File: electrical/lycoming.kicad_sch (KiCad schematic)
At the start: 30 parts

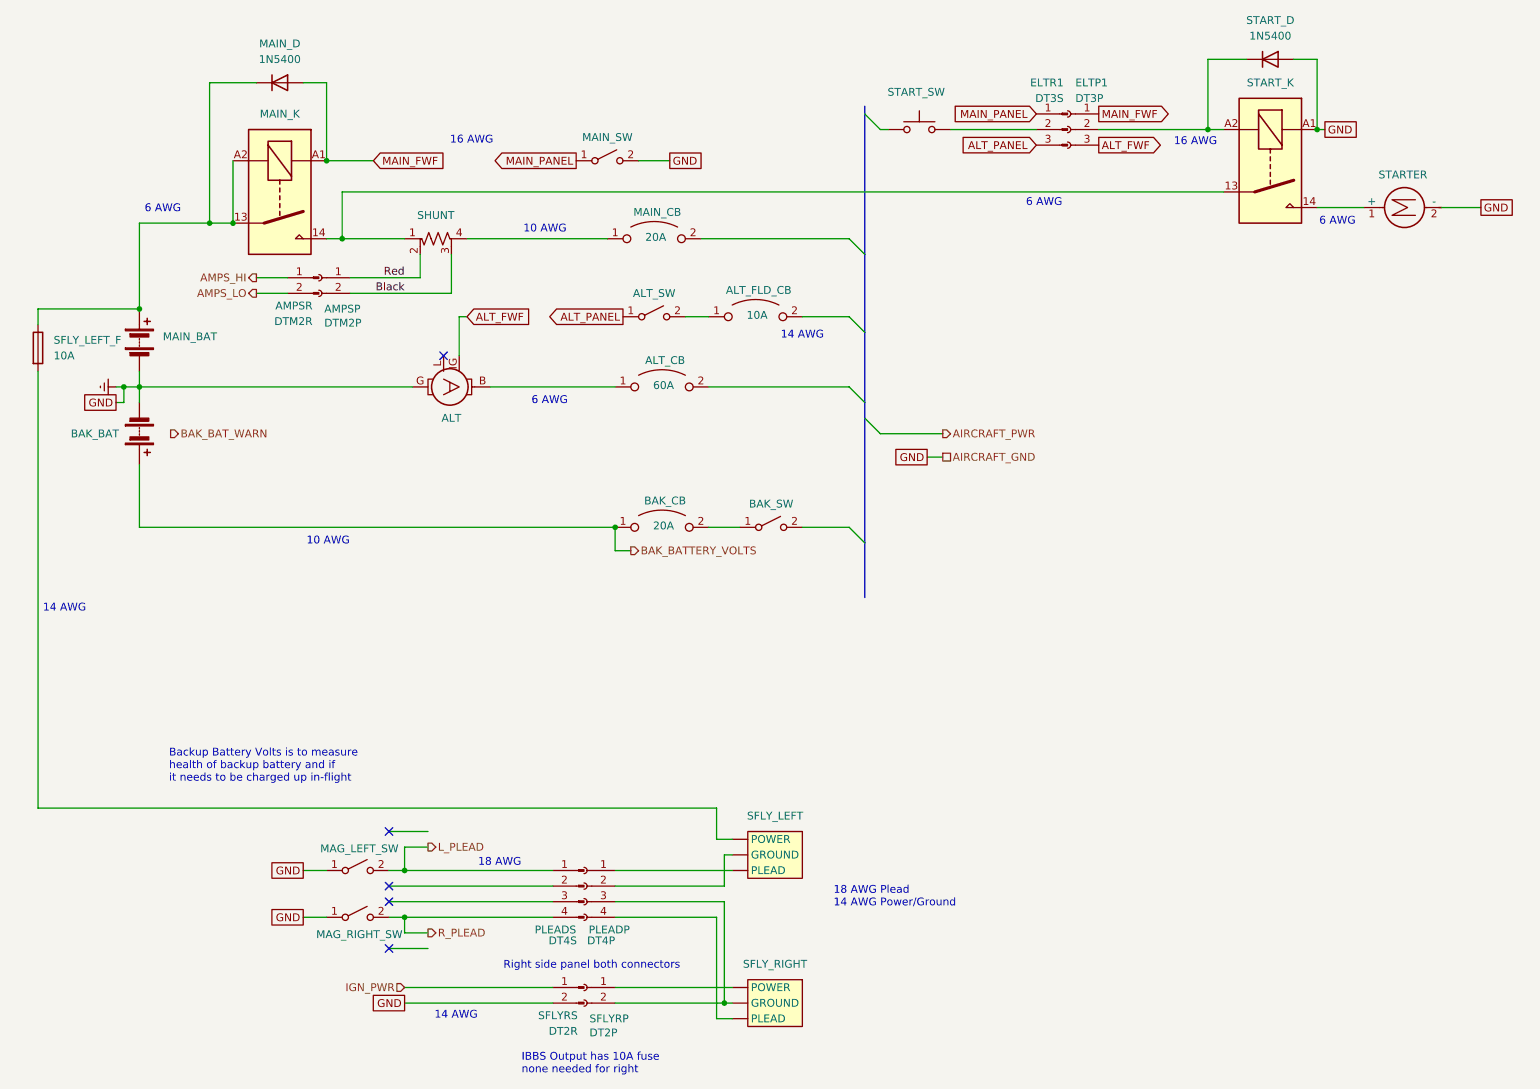
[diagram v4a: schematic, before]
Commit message: Assumed engine connector is sufficient for wiring on bench..
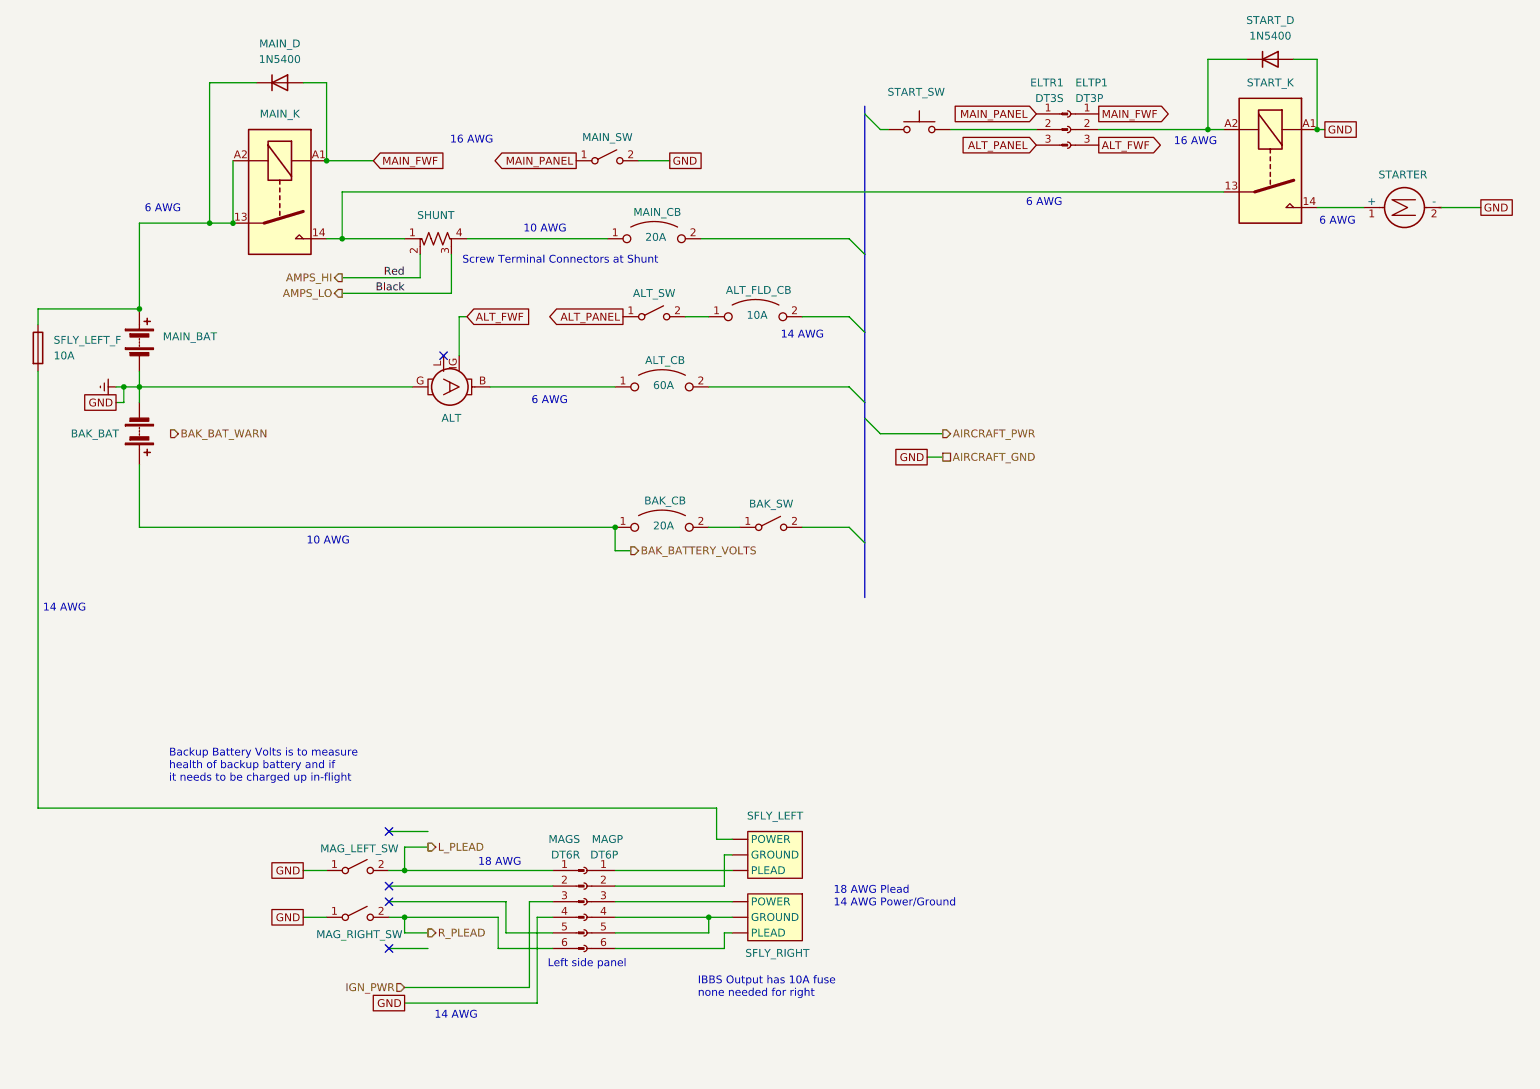
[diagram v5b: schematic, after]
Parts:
- removed AMPSP: DTM2P, symbol Connector:Conn_01x02_Socket
- removed AMPSR: DTM2R, symbol Connector:Conn_01x02_Pin
- removed PLEADP: DT4P, symbol Connector:Conn_01x04_Socket
- removed PLEADS: DT4S, symbol Connector:Conn_01x04_Pin
- removed SFLYRP: DT2P, symbol Connector:Conn_01x02_Socket
- removed SFLYRS: DT2R, symbol Connector:Conn_01x02_Pin
- added MAGP: DT6P, symbol Connector:Conn_01x06_Socket
- added MAGS: DT6R, symbol Connector:Conn_01x06_Pin
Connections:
- net Black is gone; now on net AMPS_LO: SHUNT.3
- net Red is gone; now on net AMPS_HI: SHUNT.2
- net Earth: now also MAGS.4 (Pin_4)
- net IGN_PWR: now also MAGS.3 (Pin_3)
- net L_PLEAD: now also MAGS.1 (Pin_1)
- net R_PLEAD: now also MAGS.6 (Pin_6)
- net at SFLY_RIGHT. (PLEAD): now also MAGP.6 (Pin_6)
- net at SFLY_LEFT. (PLEAD): now also MAGP.2 (Pin_2)
- new net: MAGP.3 (Pin_3), SFLY_RIGHT. (PLEAD)
- new net: MAGP.4 (Pin_4), MAGP.5 (Pin_5), SFLY_RIGHT. (PLEAD)
- new net: MAGP.1 (Pin_1), SFLY_LEFT. (PLEAD)
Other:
- note added: "Left side panel"
- note added: "Screw Terminal Connectors at Shunt"
- note removed: "Right side panel both connectors"
- moved on the sheet: SFLY_RIGHT
